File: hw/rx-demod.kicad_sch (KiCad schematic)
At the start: 0 parts

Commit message: Starting design of RF front end and demod
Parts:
- added C1, C2, C7: .1uF, symbol Device:C
- added C3, C8: 100pF, symbol Device:C
- added FB1, FB2: FerriteBead_Small, symbol Device:FerriteBead_Small
- added R1, R5: 787, symbol Device:R_US
- added R17, R18: 20, symbol Device:R_US
- added U1: AD8333ACPZ-REEL7, AD8333ACPZ-REEL7:QFN50P500X475X100-33N, symbol AD8333ACPZ-REEL7:AD8333ACPZ-REEL7
- added U3, U5: AD8021ARMZ, PCM_Package_SO_AKL:MSOP-8_3x3mm_P0.65mm, symbol PCM_Amplifier_Operational_AKL:AD8021ARMZ
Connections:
- net RxI: now also R1.2, U3.6
- net RxQ: now also R5.2, U5.6
- new net: R5.1, U1.22 (Q1NO), U5.2 (-)
- new net: C1.1, U1.6 (LODC)
- new net: C7.1, C8.1, FB2.1
- new net: C2.1, C3.1, FB1.2, U1.11 (VPOS), U1.14 (VPOS), U1.27 (VPOS), U1.30 (VPOS)
- new net: FB2.2, U1.21 (VNEG)
- new net: R1.1, U1.25 (I1NO), U3.2 (-)
- new net: R18.2, U1.28 (RF1N)
- new net: R17.2, U1.29 (RF1P)
- new net +5VA: FB1.1
- new net GND: C1.2, C2.2, C3.2, C7.2, C8.2, U1.1 (PH12), U1.10 (PH20), U1.15 (RSET), U1.2 (PH13), U1.20 (COMM), U1.26 (ENBL), U1.3 (COMM), U1.31 (PH10), U1.32 (PH11), U1.7 (PH23), U1.8 (PH22), U1.9 (PH21), U3.1 (GND), U3.3 (+), U5.1 (GND), U5.3 (+)
- new net RxRFN: R18.1
- new net RxRFP: R17.1
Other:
- title: (none) -> Receiver Demodulator

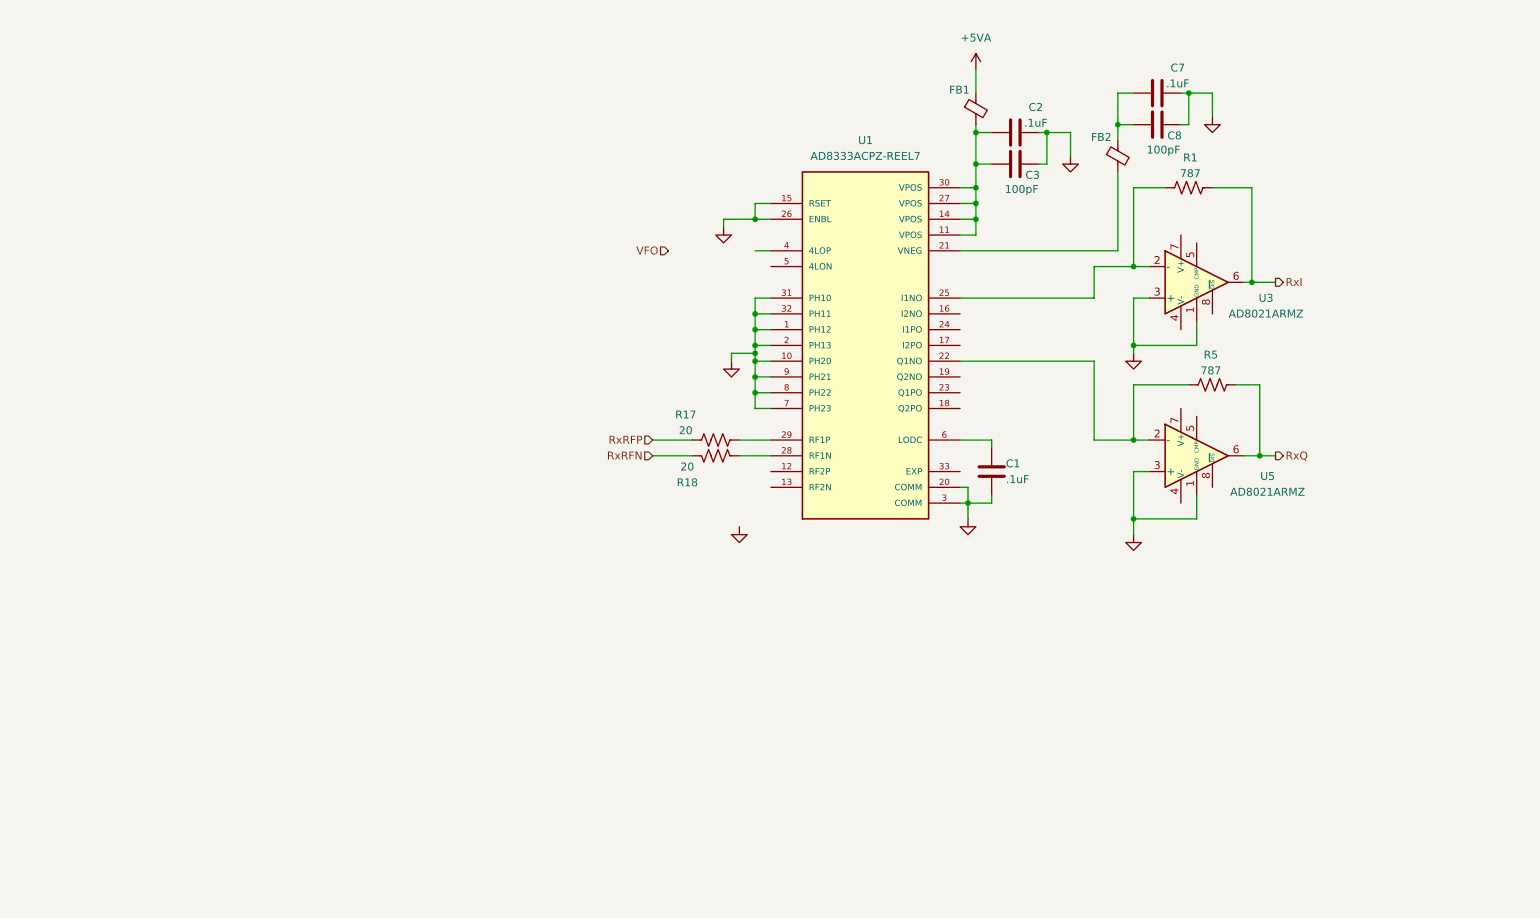
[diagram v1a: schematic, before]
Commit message: Rx path is getting closer. Differential LO outputs from VFO. Clean up.
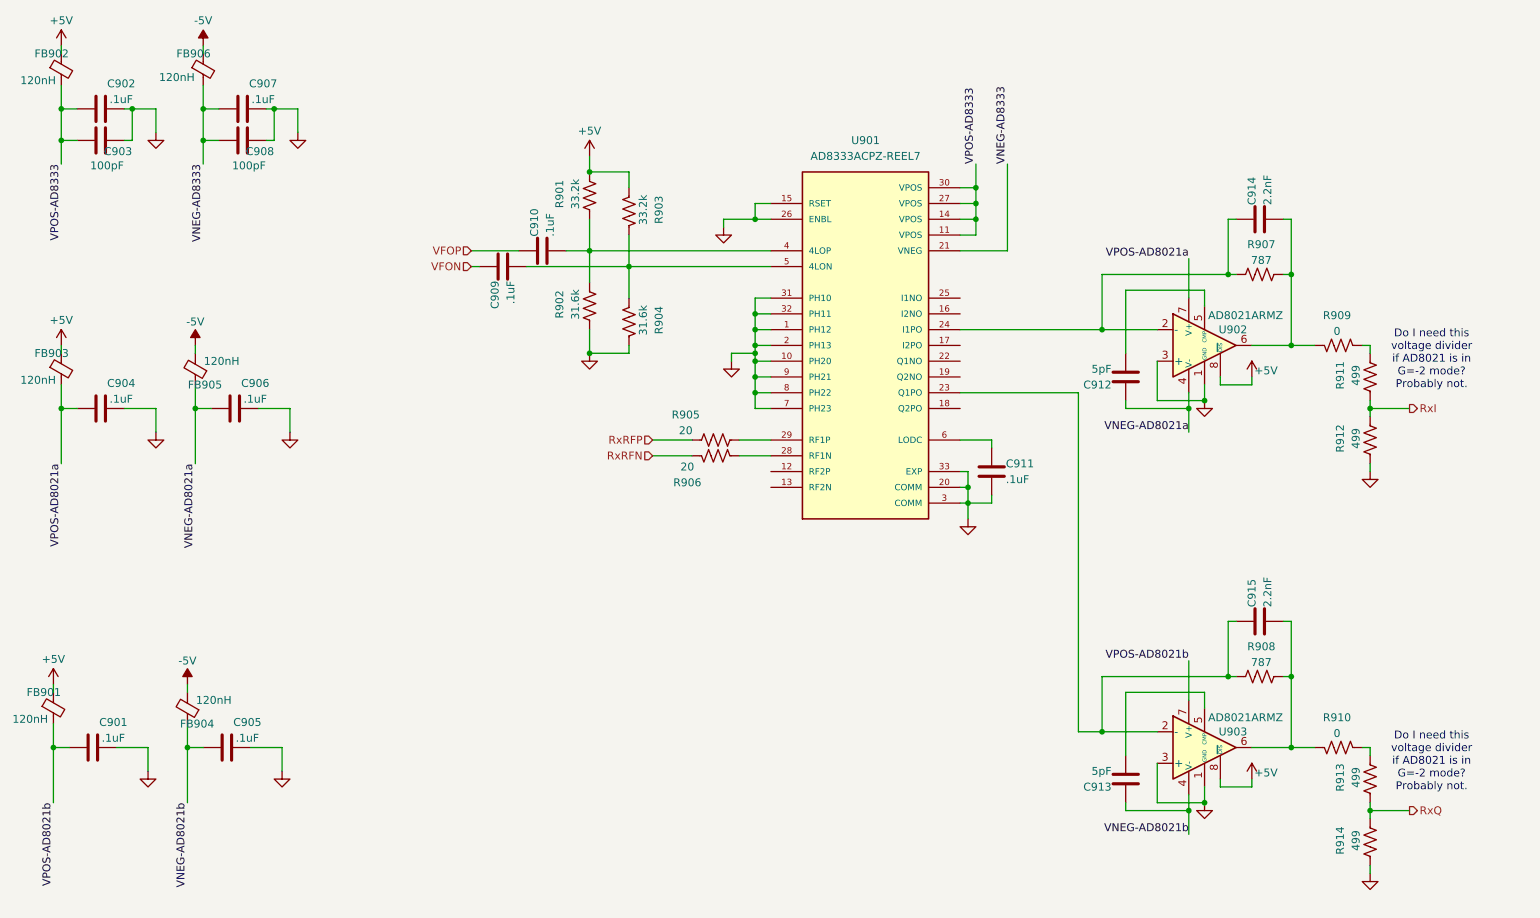
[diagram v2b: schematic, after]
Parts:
- removed R5: 787, symbol Device:R_US
- removed U5: AD8021ARMZ, PCM_Package_SO_AKL:MSOP-8_3x3mm_P0.65mm, symbol PCM_Amplifier_Operational_AKL:AD8021ARMZ
- added C901, C904, C905, C906, C909, C910: .1uF, symbol Device:C
- added C912, C913: 5pF, symbol Device:C
- added C914, C915: 2.2nF, symbol Device:C
- added FB901, FB903, FB904, FB905: 120nH, symbol Device:FerriteBead_Small
- added R901, R903: 33.2k, symbol Device:R_US
- added R902, R904: 31.6k, symbol Device:R_US
- added R908: 787, symbol Device:R_US
- added R909, R910: 0, symbol Device:R_US
- added R911, R912, R913, R914: 499, symbol Device:R_US
- added U903: AD8021ARMZ, PCM_Package_SO_AKL:MSOP-8_3x3mm_P0.65mm, symbol PCM_Amplifier_Operational_AKL:AD8021ARMZ
- FB902: renamed from FB1; value FerriteBead_Small -> 120nH
- FB906: renamed from FB2; value FerriteBead_Small -> 120nH
- renumbered C2 to C902, C3 to C903, C7 to C907, C8 to C908, C1 to C911, R17 to R905, R18 to R906, R1 to R907, U1 to U901, U3 to U902
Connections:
- net +5VA is gone; now on net +5V: FB902.1
- net GND: now also U901.33 (EXP), C901.2, C904.2, C905.2, C906.2, R902.1, R904.1, R912.1, R914.1, U903.1 (GND), U903.3 (+)
- net RxI: now also R911.1, R912.2; no longer R907.2, U902.6
- net RxQ: now also R913.1, R914.2
- net VNEG-AD8333: now reaches C907.1, C908.1
- net VNEG-AD8333: now also FB906.2, U901.21 (VNEG); no longer FB906.1
- net VPOS-AD8333: now reaches C902.1, C903.1, FB902.2, U901.11 (VPOS), U901.14 (VPOS), U901.27 (VPOS), U901.30 (VPOS)
- net at U901.23 (Q1PO): now also C915.1, R908.1, U903.2 (-)
- net at U901.24 (I1PO): now also R907.1, U902.2 (-), C914.1
- net at U901.4 (4LOP): now also C910.2, R901.1, R902.2
- net at U901.5 (4LON): now also C909.2, R903.1, R904.2
- net VNEG-AD8021a: now reaches U902.4 (V-)
- net VNEG-AD8021a: now also C906.1, C912.1, FB905.1
- net at U902.5 (CMP): now also C912.2
- net VPOS-AD8021a: now reaches U902.7 (V+)
- net VPOS-AD8021a: now also C904.1, FB903.2
- net +5V: now reaches U902.8 (~{DIS})
- net +5V: now also FB901.1, FB903.1, R901.2, R903.2, U903.8 (~{DIS})
- new net: C915.2, R908.2, R910.2, U903.6
- new net: R910.1, R913.2
- new net: C913.2, U903.5 (CMP)
- new net: R909.1, R911.2
- new net: C914.2, R907.2, R909.2, U902.6
- new net -5V: FB904.2, FB905.2, FB906.1
- new net VFON: C909.1
- new net VFOP: C910.1
- new net VNEG-AD8021b: C905.1, C913.1, FB904.1, U903.4 (V-)
- new net VPOS-AD8021b: C901.1, FB901.2, U903.7 (V+)
- now unconnected: U901.25 (I1NO)
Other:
- note added: "Do I need this voltage divider if AD8021 is in G=-2 mode? Probably not."
- moved on the sheet: C902, C903, C907, C908, FB902, FB906, R907, U902

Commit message: Working on multi-band BPF and switching
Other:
- company: SoftShack -> WB7NAB
- title: Receiver Demodulator -> ${title}
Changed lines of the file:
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@@
 	(generator "eeschema")
 	(generator_version "9.0")
-	(paper "A")
+	(paper "USLetter")
 	(title_block
-		(title "Receiver Demodulator")
-		(date "2025-03-26")
-		(company "SoftShack")
+		(title "${title}")
+		(date "2025-08-10")
+		(company "WB7NAB")
 		(comment 1 "Alan Mimms")
-		(comment 2 "WB7NAB")
 	)
 	(text "Do I need this\nvoltage divider\nif AD8021 is in\nG=-2 mode?\nProbably not."

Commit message: Starting to build BPFs for 7 bands
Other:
- title: ${title} -> Rx Demod
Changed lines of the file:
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@@
 	(paper "USLetter")
 	(title_block
-		(title "${title}")
+		(title "Rx Demod")
 		(date "2025-08-10")
 		(company "WB7NAB")
